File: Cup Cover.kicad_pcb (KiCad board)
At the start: 2 copper layers, 46 x 35.5 mm, 7 parts, among them SW1 SW_Push, SW2 SW_Reed

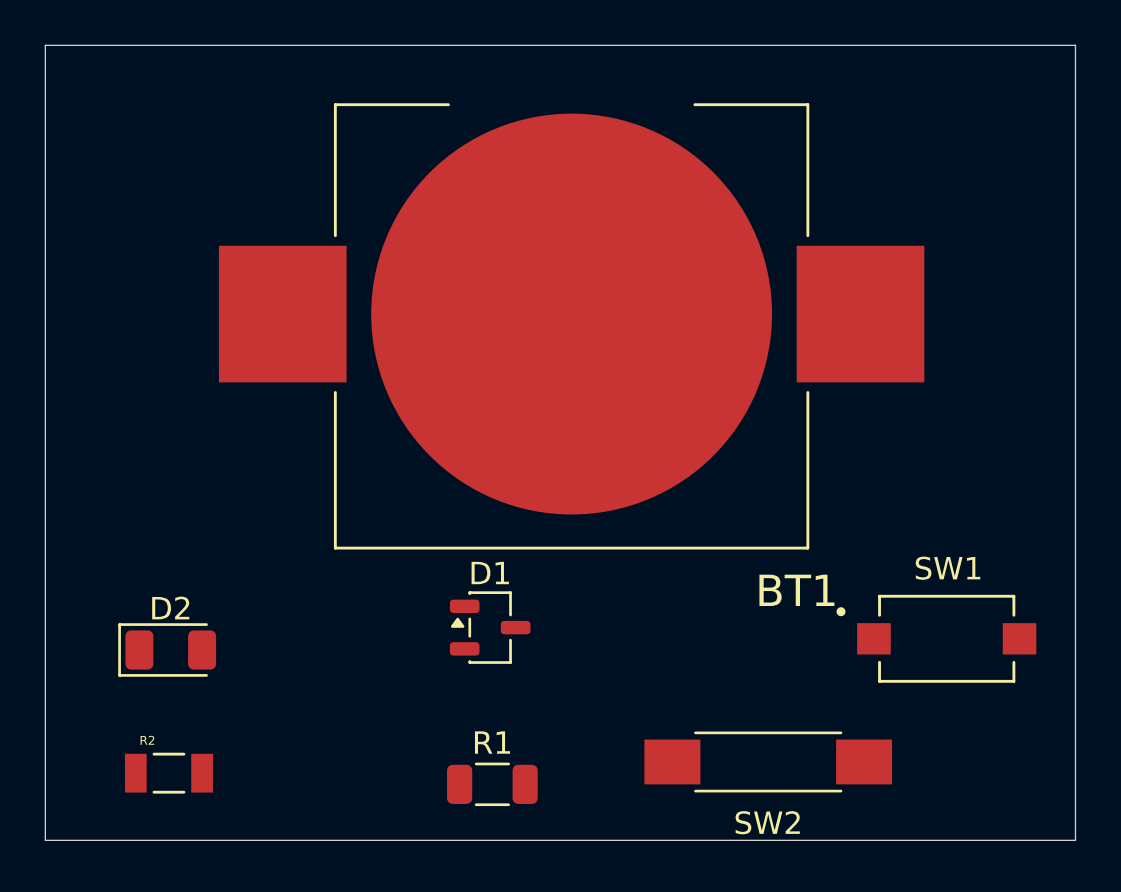
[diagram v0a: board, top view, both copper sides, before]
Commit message: board review 1 (battery footp, reed sw)
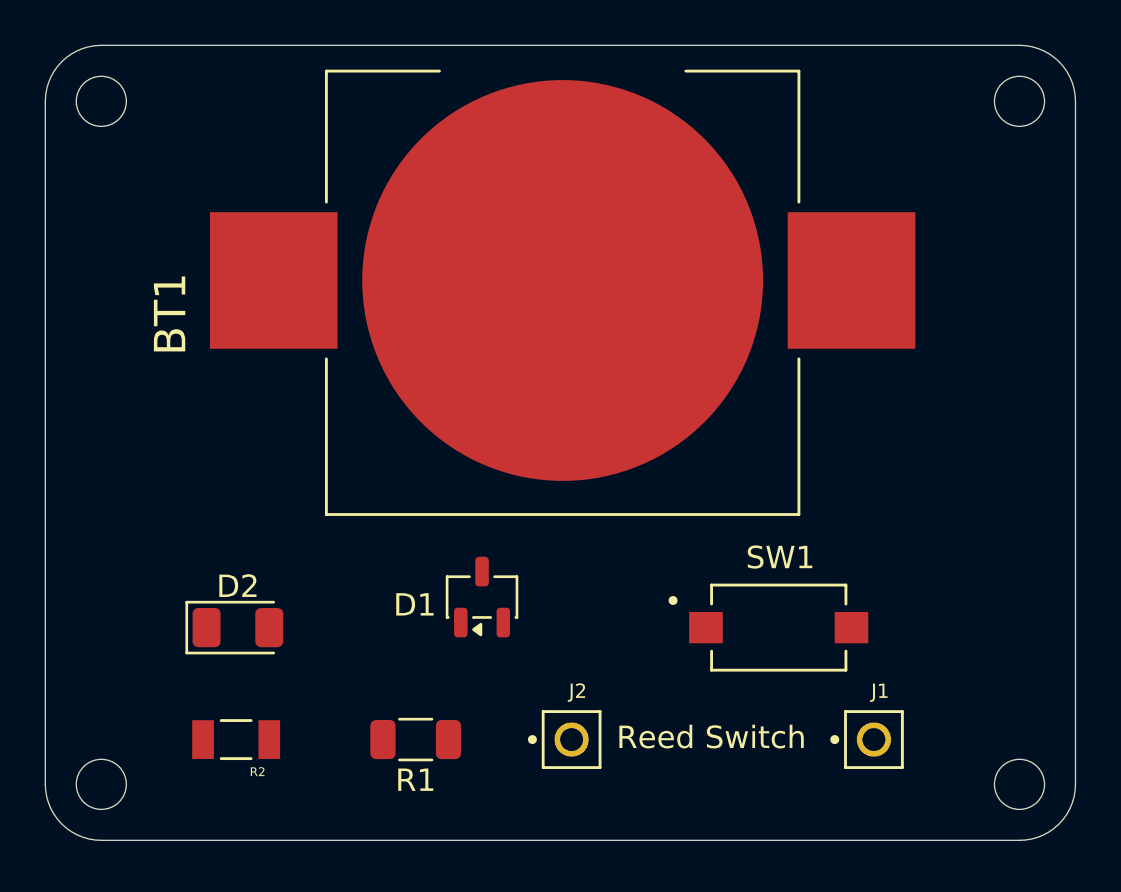
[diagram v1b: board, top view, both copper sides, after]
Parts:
- removed SW2: SW_Reed, Button_Switch_SMD:SW_SPST_REED_CT05-XXXX-G1
- added J1: Conn_01x01_Pin, PH1-01-UA:ADAM-TECH_PH1-01-UA, F.Cu at (89.5, 67.0)
- added J2: Conn_01x01_Pin, PH1-01-UA:ADAM-TECH_PH1-01-UA, F.Cu at (76.0, 67.0)
- moved SW1 7.52 mm to (85.2, 62.0)
- moved R1 3.97 mm to (69.0, 67.0), turned to 180 degrees
- moved R2 3.35 mm to (61.0, 67.0), turned to 180 degrees
- moved D2 3.16 mm to (61.1, 62.0)
- moved BT1 1.55 mm to (75.6, 46.5)
- moved D1 1.41 mm to (72.0, 60.6), turned to 90 degrees
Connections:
- net Net-(BT1--) renamed GND
- net Net-(D1-A) renamed REED_SW_POS
- R1 pad 1: Net-(R1-Pad1) -> REED_SW_NEG
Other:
- outline, holes or cut-outs redrawn
- board text added: "Reed Switch"

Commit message: 2/20 Routed PCB
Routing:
- net Net-(BT1-+): track 0.00 -> 44.0 mm
- net GND: track 0.00 -> 41.1 mm
- net REED_SW_POS: track 0.00 -> 23.8 mm
- net Net-(D1-K): track 0.00 -> 12.6 mm
- net Net-(D1-G): track 0.00 -> 10.1 mm
- net Net-(D2-A): track 0.00 -> 6.23 mm
- net REED_SW_NEG: track 0.00 -> 5.50 mm
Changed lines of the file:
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@@
 			(outputformat 1)
 			(mirror no)
-			(drillshape 1)
+			(drillshape 0)
 			(scaleselection 1)
-			(outputdirectory "")
+			(outputdirectory "Gerbers/")
 		)
 	)
@@
 			(effects
 				(font
-					(size 0.393701 0.393701)
-					(thickness 0.15)
+					(size 0.6 0.6)
+					(thickness 0.098425)
 				)
 			)
@@
 			(effects
 				(font
-					(size 1 1)
-					(thickness 0.15)
+					(size 0.6 0.6)
+					(thickness 0.098425)
 				)
 			)
@@
 	)
 	(gr_line
+		(start 64 62)
+		(end 65 62)
+		(stroke
+			(width 0.1)
+			(type default)
+		)
+		(layer "F.SilkS")
+	)
+	(gr_line
+		(start 64.5 61.5)
+		(end 64.5 62.5)
+		(stroke
+			(width 0.1)
+			(type default)
+		)
+		(layer "F.SilkS")
+	)
+	(gr_line
 		(start 55 71.5)
 		(end 96 71.5)
@@
 	(dimension
 		(type orthogonal)
-		(layer "Edge.Cuts")
+		(layer "F.Fab")
 		(pts
 			(xy 98.5 43) (xy 52.5 43.5)
@@
 		(gr_text "46"
 			(at 75.5 26.85 0)
-			(layer "Edge.Cuts")
+			(layer "F.Fab")
 			(effects
 				(font
@@
 	(dimension
 		(type orthogonal)
-		(layer "Edge.Cuts")
+		(layer "F.Fab")
 		(pts
 			(xy 59 36) (xy 58.805 71.5)
@@
 		(gr_text "35.5"
 			(at 34.85 53.75 90)
-			(layer "Edge.Cuts")
+			(layer "F.Fab")
 			(effects
 				(font
@@
 		)
 	)
+	(segment
+		(start 59.549 61.849)
+		(end 59.549 43.149)
+		(width 0.2)
+		(layer "F.Cu")
+		(net 1)
+	)
+	(segment
+		(start 65.148 37.55)
+		(end 66.65 37.55)
+		(width 0.2)
+		(layer "F.Cu")
+		(net 1)
+	)
+	(segment
+		(start 59.549 43.149)
+		(end 65.148 37.55)
+		(width 0.2)
+		(layer "F.Cu")
+		(net 1)
+	)
+	(segment
+		(start 59.7 62)
+		(end 59.549 61.849)
+		(width 0.2)
+		(layer "F.Cu")
+		(net 1)
+	)
+	(segment
+		(start 66.65 37.55)
+		(end 75.6 46.5)
+		(width 0.2)
+		(layer "F.Cu")
+		(net 1)
+	)
+	(segment
+		(start 75.6 46.5)
+		(end 75.55 46.45)
+		(width 0.2)
+		(layer "F.Cu")
+		(net 1)
+	)
+	(segment
+		(start 88.5 46.5)
+		(end 88.5 55.5)
+		(width 0.2)
+		(layer "F.Cu")
+		(net 2)
+	)
+	(segment
+		(start 78 62)
+		(end 82 62)
+		(width 0.2)
+		(layer "F.Cu")
+		(net 2)
+	)
+	(segment
+		(start 62.7 46.5)
+		(end 62.7 46.7)
+		(width 0.2)
+		(layer "F.Cu")
+		(net 2)
+	)
+	(segment
+		(start 62.7 46.7)
+		(end 78 62)
+		(width 0.2)
+		(layer "F.Cu")
+		(net 2)
+	)
+	(segment
+		(start 88.5 55.5)
+		(end 82 62)
+		(width 0.2)
+		(layer "F.Cu")
+		(net 2)
+	)
+	(segment
+		(start 70 59.5)
+		(end 62.5 67)
+		(width 0.2)
+		(layer "F.Cu")
+		(net 3)
+	)
+	(segment
+		(start 72 59.5)
+		(end 70 59.5)
+		(width 0.2)
+		(layer "F.Cu")
+		(net 3)
+	)
+	(segment
+		(start 71.9865 60.8115)
+		(end 72.95 61.775)
+		(width 0.2)
+		(layer "F.Cu")
+		(net 4)
+	)
+	(segment
+		(start 67.575 63.945532)
+		(end 70.709032 60.8115)
+		(width 0.2)
+		(layer "F.Cu")
+		(net 4)
+	)
+	(segment
+		(start 67.575 67)
+		(end 67.575 63.945532)
+		(width 0.2)
+		(layer "F.Cu")
+		(net 4)
+	)
+	(segment
+		(start 70.709032 60.8115)
+		(end 71.9865 60.8115)
+		(width 0.2)
+		(layer "F.Cu")
+		(net 4)
+	)
+	(segment
+		(start 59.54 64.96)
+		(end 62.5 62)
+		(width 0.2)
+		(layer "F.Cu")
+		(net 5)
+	)
+	(segment
+		(start 59.54 67)
+		(end 59.54 64.96)
+		(width 0.2)
+		(layer "F.Cu")
+		(net 5)
+	)
+	(segment
+		(start 72.276 63.001)
+		(end 71.05 61.775)
+		(width 0.2)
+		(layer "F.Cu")
+		(net 6)
+	)
+	(segment
+		(start 88.5 62)
+		(end 88.5 66)
+		(width 0.2)
+		(layer "F.Cu")
+		(net 6)
+	)
+	(segment
+		(start 88.5 66)
+		(end 89.5 67)
+		(width 0.2)
+		(layer "F.Cu")
+		(net 6)
+	)
+	(segment
+		(start 88.5 62)
+		(end 87.499 63.001)
+		(width 0.2)
+		(layer "F.Cu")
+		(net 6)
+	)
+	(segment
+		(start 87.499 63.001)
+		(end 72.276 63.001)
+		(width 0.2)
+		(layer "F.Cu")
+		(net 6)
+	)
+	(segment
+		(start 76 67)
+		(end 70.5 67)
+		(width 0.2)
+		(layer "F.Cu")
+		(net 7)
+	)
 	(embedded_fonts no)
